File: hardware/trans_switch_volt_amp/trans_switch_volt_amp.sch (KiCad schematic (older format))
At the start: 22 parts, among them J1 Ard_6_pin, J2 DAC0_arduino, J3 to biopac, J4 To biopac, J5 DAC1_arduino, J6 Ard_5_pin, Q1 BC182L_NPN, Q2 BC182L_NPN, U1 LM741, U2 LM741

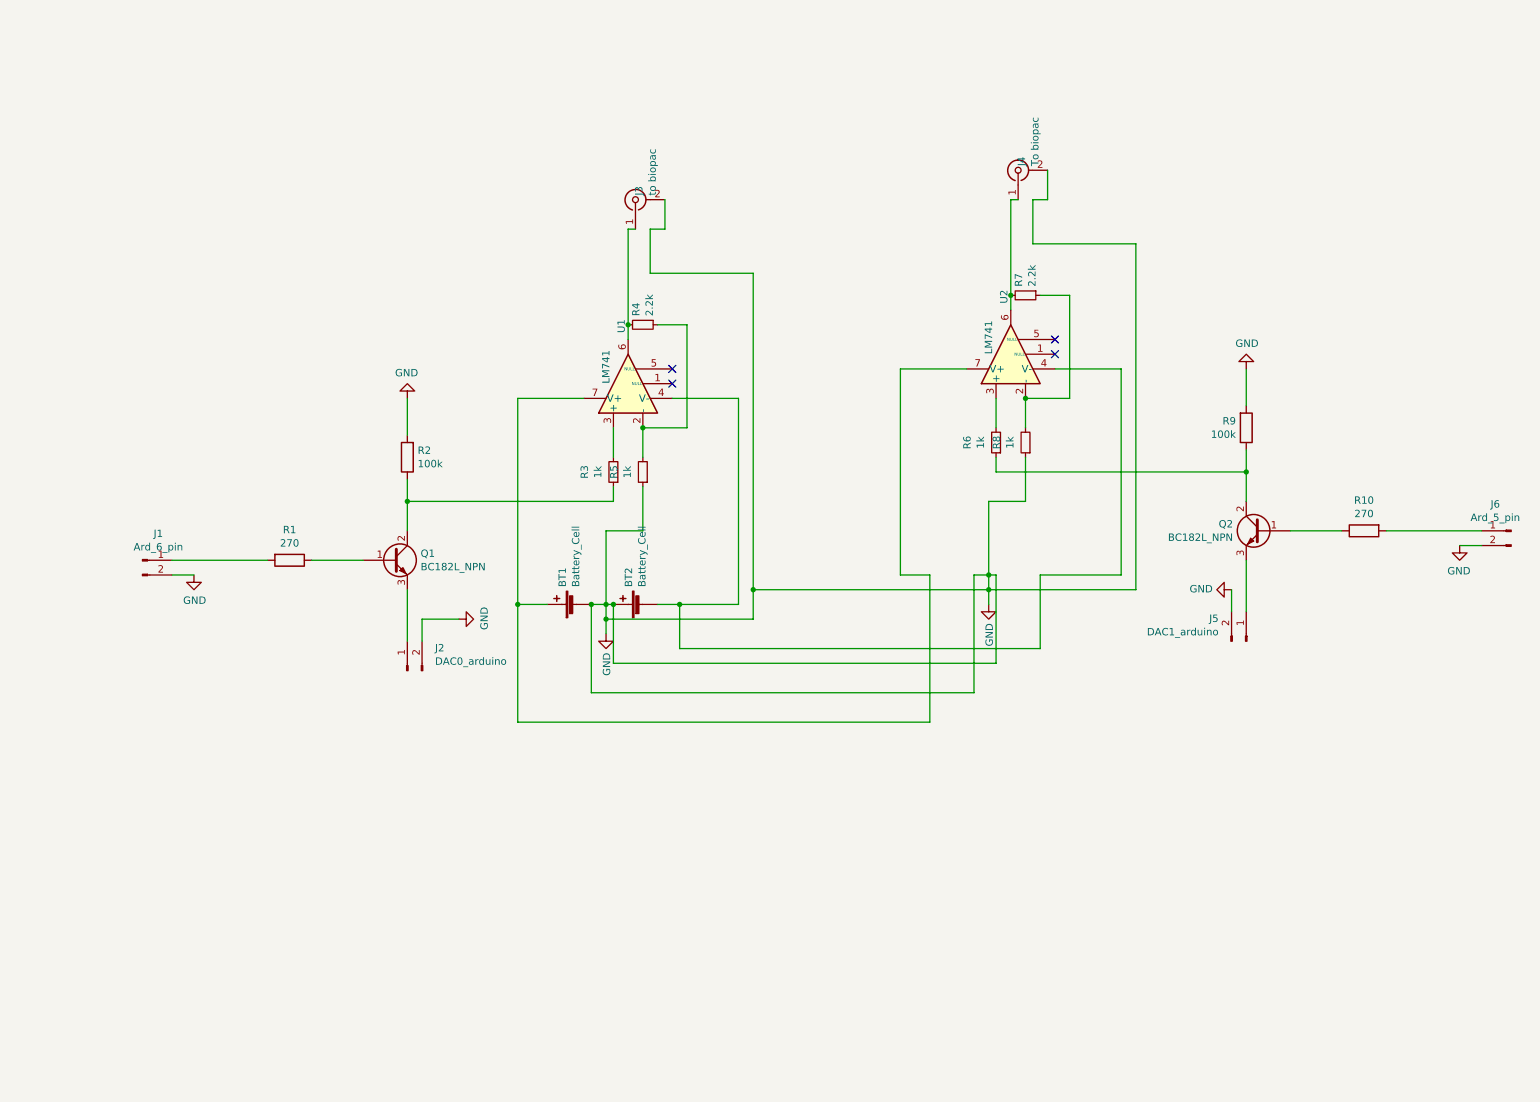
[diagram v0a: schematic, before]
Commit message: created shield for the amplifier system
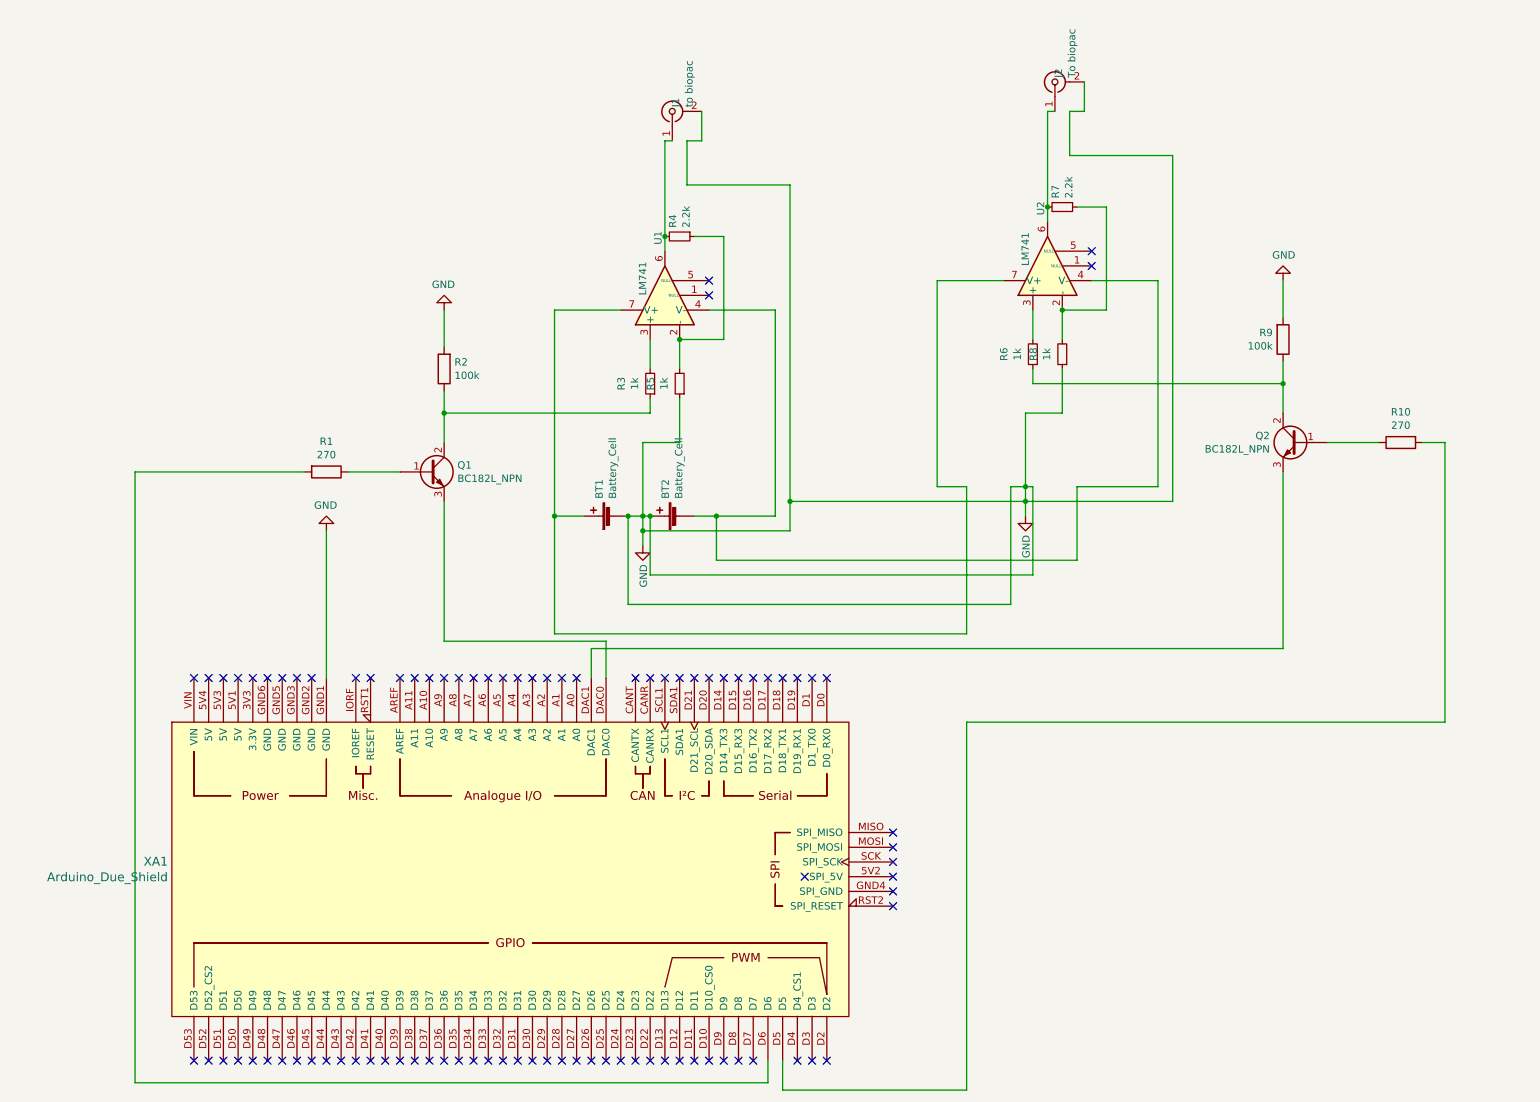
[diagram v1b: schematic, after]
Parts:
- removed J1: Ard_6_pin, symbol Connector:Conn_01x02_Male
- removed J2: DAC0_arduino, Connector_PinHeader_2.54mm:PinHeader_1x07_P2.54mm_Vertical, symbol Connector:Conn_01x02_Male
- removed J5: DAC1_arduino, symbol Connector:Conn_01x02_Male
- removed J6: Ard_5_pin, symbol Connector:Conn_01x02_Male
- added XA1: Arduino_Due_Shield, Arduino:Arduino_Due_Shield, symbol Arduino:Arduino_Due_Shield
- BT1, BT2: footprint (none) -> Battery:BatteryHolder_Eagle_12BH611-GR
- Q1, Q2: footprint (none) -> Package_TO_SOT_THT:TO-92L_Wide
- R1, R10, R2, R3, R4, R5, R6, R7, R8, R9: footprint (none) -> Resistor_THT:R_Box_L13.0mm_W4.0mm_P9.00mm
- U1, U2: footprint (none) -> Package_DIP:DIP-8_W7.62mm
- renumbered J3 to J1, J4 to J2
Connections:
- net GND: now also XA1.GND1 (GND)
- net at Q1.3 (E): now also XA1.DAC0
- net at R1.2: now also XA1.D6
- net at Q2.3 (E): now also XA1.DAC1
- net at R10.2: now also XA1.D5
- no-connect marks 4 -> 91
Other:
- moved on the sheet: BT1, BT2, J1, J2, Q1, Q2, R1, R10, R2, R3, R4, R5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
